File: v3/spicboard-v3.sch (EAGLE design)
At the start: 40 parts, among them IC1 74HC595, Q1 BC557, Q2 BC557

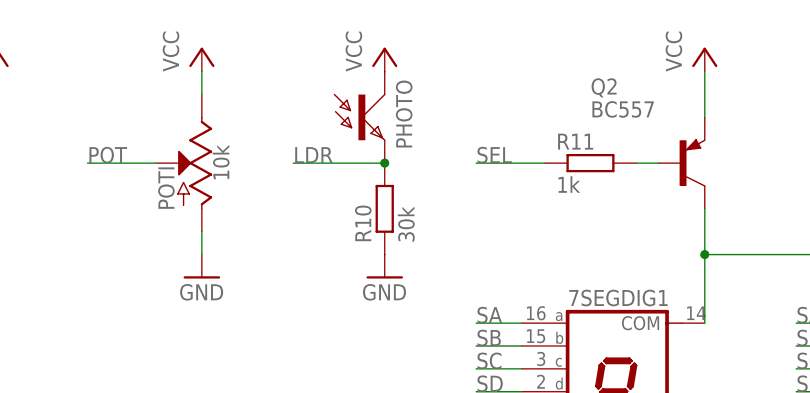
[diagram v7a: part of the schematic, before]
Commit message: SPiCboard: Kleiner Phototransistor, 7-Seg 1k Ohm
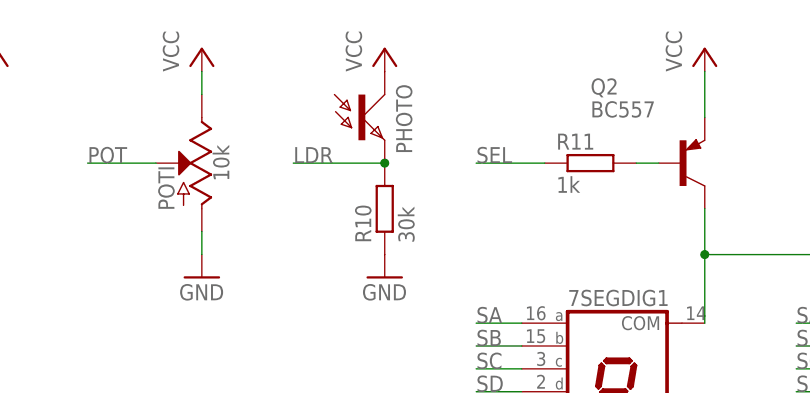
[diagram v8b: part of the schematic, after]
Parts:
- PHOTO: value PTPT5MM -> PTPT; device spicboard-v3:PTPT5MM -> spicboard-v3:PTPT
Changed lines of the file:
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@@
 <part name="P+9" library="supply1" deviceset="VCC" device=""/>
 <part name="EXT" library="SparkFun-Connectors" deviceset="CONN_03" device=""/>
-<part name="PHOTO" library="spicboard-v3" deviceset="PT" device="PT5MM" value="PTPT5MM"/>
+<part name="PHOTO" library="spicboard-v3" deviceset="PT" device="PT"/>
 </parts>
 <sheets>
@@
 <instance part="EXT" gate="J$1" x="45.72" y="-17.78" rot="R180"/>
 <instance part="PHOTO" gate="G$1" x="81.28" y="101.6" smashed="yes">
-<attribute name="NAME" x="86.868" y="98.044" size="1.778" layer="95" rot="R90"/>
+<attribute name="NAME" x="86.868" y="97.536" size="1.778" layer="95" rot="R90"/>
 </instance>
 </instances>
